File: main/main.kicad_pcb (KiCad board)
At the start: 2 copper layers, 50 parts, among them J1 RJ45, J2 RJ45, J3 Connector, USB-TYPE-C-16P, J4 Conn_01x04_Pin, J5 Conn_01x04_Pin, Q1 MMBT3904, U2 2.4GHz

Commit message: PCB Updates
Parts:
- moved J1 8.03 mm to (95.7, 50.4)
- moved J2 8.00 mm to (128.1, 50.4)
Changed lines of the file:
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@@
 	(footprint "Connector_RJ:RJ45_Amphenol_54602-x08_Horizontal"
 		(layer "F.Cu")
-		(at 120.06 50.39)
+		(at 128.06 50.39)
 		(descr "8 Pol Shallow Latch Connector, Modjack, RJ45 (https://cdn.amphenol-icc.com/media/wysiwyg/files/drawing/c-bmj-0102.pdf)")
 		(tags "RJ45")
@@
 	(footprint "Connector_RJ:RJ45_Amphenol_54602-x08_Horizontal"
 		(layer "F.Cu")
-		(at 103.75 50.39)
+		(at 95.7175 50.39)
 		(descr "8 Pol Shallow Latch Connector, Modjack, RJ45 (https://cdn.amphenol-icc.com/media/wysiwyg/files/drawing/c-bmj-0102.pdf)")
 		(tags "RJ45")

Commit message: PCB Progress
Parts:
- removed J5: Conn_01x04_Pin, Connector_PinHeader_2.54mm:PinHeader_1x04_P2.54mm_Vertical
- added H1: MountingHole, MountingHole:MountingHole_3.2mm_M3, F.Cu at (104.5, 73.5)
- added H2: MountingHole, MountingHole:MountingHole_3.2mm_M3, F.Cu at (125.5, 73.5)
- added H3: MountingHole, MountingHole:MountingHole_3.2mm_M3, F.Cu at (88.0, 30.0)
- added H4: MountingHole, MountingHole:MountingHole_3.2mm_M3, F.Cu at (141.8, 30.2)
- added J6: Conn_01x08_Pin, Connector_PinHeader_2.54mm:PinHeader_1x08_P2.54mm_Vertical, F.Cu at (123.9, 78.8)
- moved S5 108.8 mm to (139.5, 38.2), turned to -90 degrees
- moved S4 107.4 mm to (139.5, 45.0), turned to -90 degrees
- moved S3 107.3 mm to (139.5, 51.8), turned to -90 degrees
- moved S1 83.7 mm to (115.3, 49.9), turned to 180 degrees
- moved S2 83.6 mm to (115.3, 53.3), turned to 180 degrees
- moved U15 81.6 mm to (144.0, 47.0)
- moved U14 81.6 mm to (144.0, 43.2)
- moved U13 81.5 mm to (144.0, 39.5)
- moved U12 81.5 mm to (144.0, 35.7)
- moved U16 77.8 mm to (144.0, 50.7)
- moved U17 77.7 mm to (144.0, 54.5)
- moved U18 77.6 mm to (144.0, 58.2)
- moved U19 77.5 mm to (144.0, 62.0)
- moved U2 68.4 mm to (111.6, 41.3), turned to 90 degrees
- moved J3 64.8 mm to (115.0, 29.9), turned to 180 degrees
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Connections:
- U2 pad 20: unconnected-(U2-IO6-Pad20) -> /SCK
- U2 pad 21: unconnected-(U2-IO7-Pad21) -> /MOSI
- U2 pad 5: unconnected-(U2-IO2-Pad5) -> /DC
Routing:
- net /P1_1: track 0.00 -> 22.4 mm
- net /P2_7: track 0.00 -> 21.3 mm
- net /P1_3: track 0.00 -> 20.3 mm
- net /P2_8: track 0.00 -> 19.6 mm
- net /P2_5: track 0.00 -> 19.3 mm
- net /P1_2: track 0.00 -> 18.8 mm
- net /P1_5: track 0.00 -> 18.3 mm
- net /P2_3: track 0.00 -> 17.6 mm
- net /P2_6: track 0.00 -> 17.5 mm
- net /P1_7: track 0.00 -> 17.0 mm
- net /P2_1: track 0.00 -> 17.0 mm
- net /P1_4: track 0.00 -> 16.7 mm
- net /P2_4: track 0.00 -> 15.4 mm
- net /P2_2: track 0.00 -> 15.1 mm
- net /P1_6: track 0.00 -> 14.6 mm
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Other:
- board outline added: 62 x 54 mm

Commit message: PCB Progress
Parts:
- removed C10, C8: 47uF, PCM_JLCPCB:C_1206
- moved C4 115.2 mm to (140.5, 57.4), turned to 120 degrees
- moved C5 106.9 mm to (131.9, 34.7), turned to 90 degrees
- moved C9 98.5 mm to (124.5, 57.8)
- moved D1 85.6 mm to (123.6, 67.7), turned to -90 degrees
- moved C6 82.6 mm to (108.5, 51.8), turned to -90 degrees
- moved C3 77.6 mm to (102.8, 30.8)
- moved J4 74.9 mm to (107.8, 27.8), turned to -90 degrees
- moved C2 65.8 mm to (90.0, 53.4)
- moved D2 54.7 mm to (88.8, 37.8), turned to -90 degrees
- moved R2 49.3 mm to (119.1, 34.6)
- moved R5 49.2 mm to (118.4, 37.2)
- moved R1 49.1 mm to (119.1, 33.8), turned to 180 degrees
- moved C7 47.9 mm to (115.3, 56.5), turned to 90 degrees
- moved R7 43.5 mm to (114.0, 55.5)
- moved R4 41.3 mm to (111.4, 53.2), turned to 180 degrees
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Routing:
- net +5V: track 0.00 -> 242.0 mm, vias 0 -> 8
- net +3.3V: track 0.00 -> 91.7 mm, vias 0 -> 4
- net Net-(U11-DO): track 0.00 -> 73.8 mm, vias 0 -> 5
- net Net-(U10-DO): track 0.00 -> 72.4 mm, vias 0 -> 5
- net /WS2812: track 0.00 -> 67.9 mm, vias 0 -> 4
- net GND: track 1.27 -> 62.8 mm, vias 1 -> 48
- net /MOSI: track 0.00 -> 46.1 mm, vias 0 -> 3
- net /SCK: track 0.00 -> 44.7 mm, vias 0 -> 1
- net /SPK: track 0.00 -> 36.2 mm, vias 0 -> 2
- net /EN: track 0.00 -> 33.7 mm, vias 0 -> 2
- net /DC: track 0.00 -> 32.9 mm, vias 0 -> 2
- net /BTN1: track 0.00 -> 32.6 mm, vias 0 -> 2
- net /BTN2: track 0.00 -> 31.0 mm, vias 0 -> 2
- net /BOOT: track 0.00 -> 30.8 mm, vias 0 -> 2
- net /BTN3: track 0.00 -> 28.7 mm, vias 0 -> 2
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- added copper zone on B.Cu, net GND
- added copper zone on F.Cu, net GND

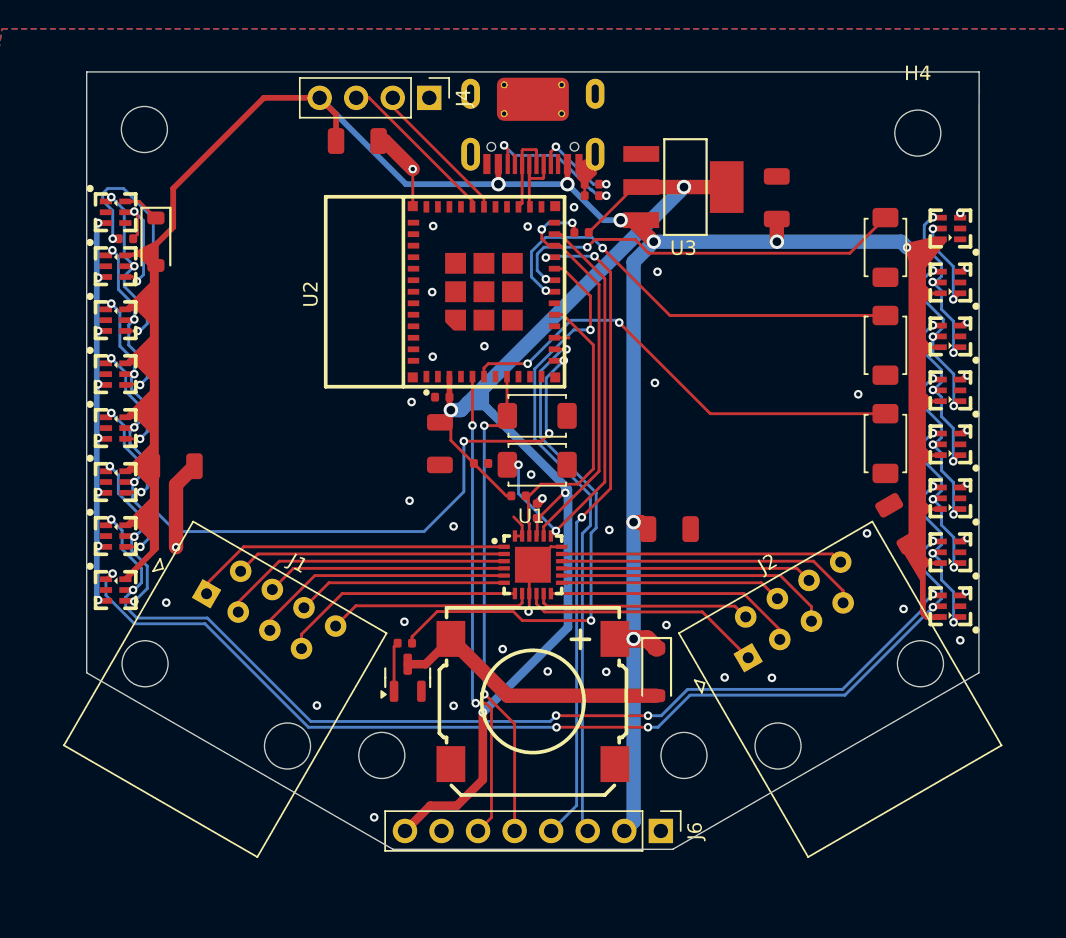
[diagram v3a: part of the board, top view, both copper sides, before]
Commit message: Nearly done, but found glaring issue with right LEDs...
They are too low...
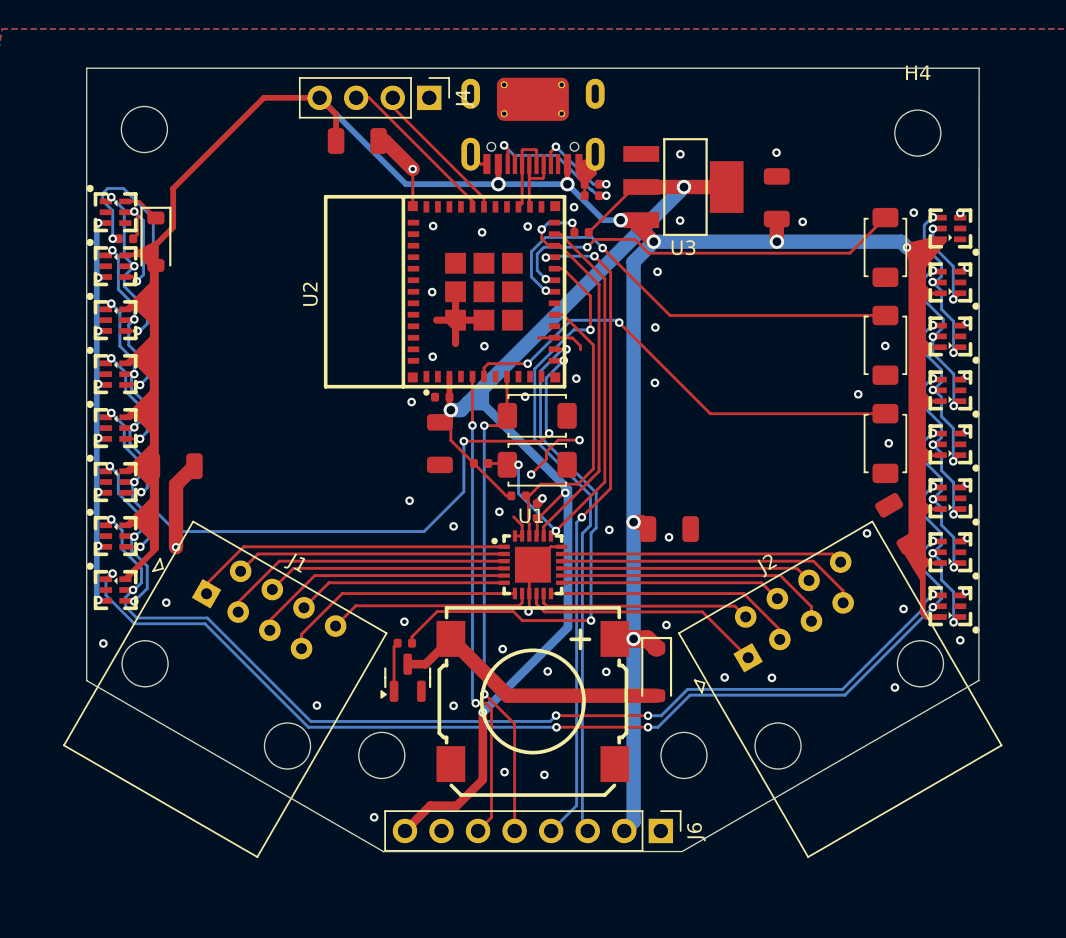
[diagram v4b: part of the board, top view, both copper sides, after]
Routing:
- net GND: track 62.8 -> 78.3 mm, vias 48 -> 66
- net /BOOT: track 30.8 -> 32.1 mm
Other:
- board size 62 x 54 mm -> 62 x 54.4 mm

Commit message: pcb updates
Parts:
- moved U12 1.15 mm to (144.0, 62.0)
- moved U13 1.15 mm to (144.0, 58.2)
- moved U14 1.15 mm to (144.0, 54.5)
- moved U15 1.15 mm to (144.0, 50.7)
- moved U16 1.15 mm to (144.0, 47.0)
- moved U17 1.15 mm to (144.0, 43.2)
- moved U18 1.15 mm to (144.0, 39.5)
- moved U19 1.15 mm to (144.0, 35.7)
- moved C4 0.06 mm to (140.5, 57.5)
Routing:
- net Net-(U10-DO): track 72.4 -> 73.6 mm
- net Net-(U11-DO): track 73.8 -> 74.9 mm
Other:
- board text added: "Terminator"
